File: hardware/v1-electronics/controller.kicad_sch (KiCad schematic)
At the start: 35 parts, among them IC1 IS31FL3733-QFLS4-TR, IC2 IS31FL3733-QFLS4-TR, J2 Conn_01x03, U1 MDBT50Q-1MV2

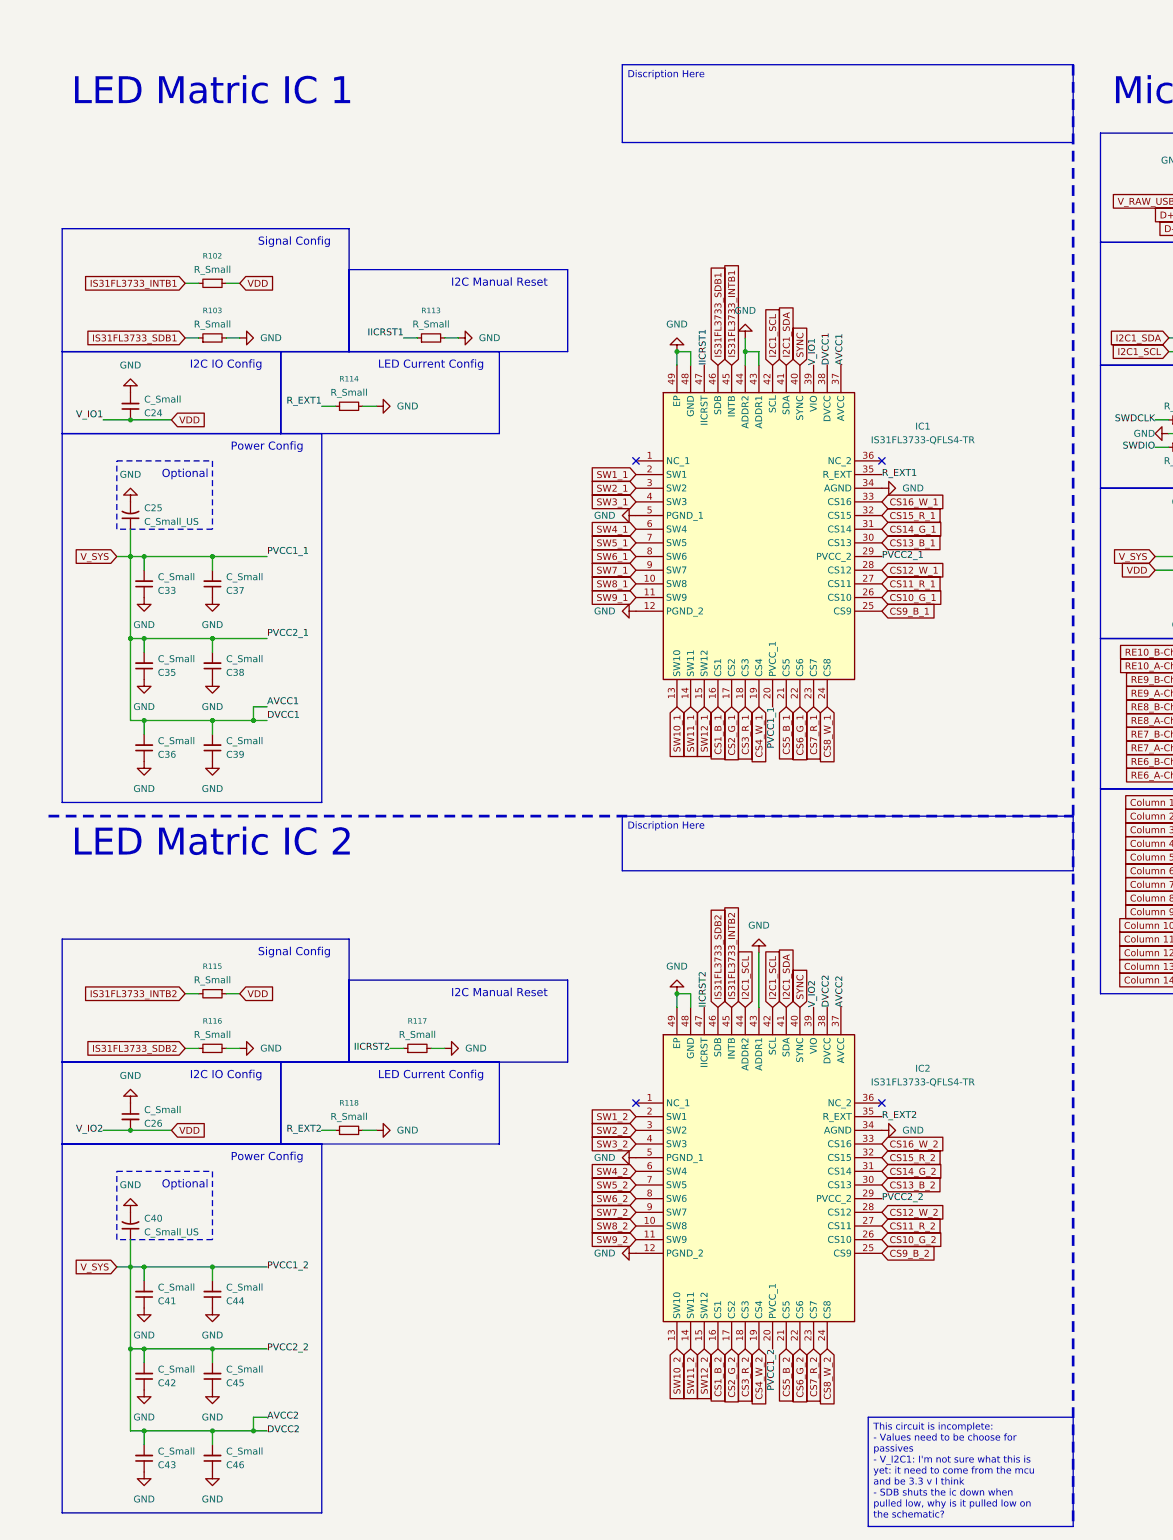
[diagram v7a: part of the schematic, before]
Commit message: fix(v1 hardware): fixed the matrix circuit
the change in LED Matrix Driver results in a need to change how we
wire the matrix. this diff accounts for that.

i needed to use a script to rename labels.
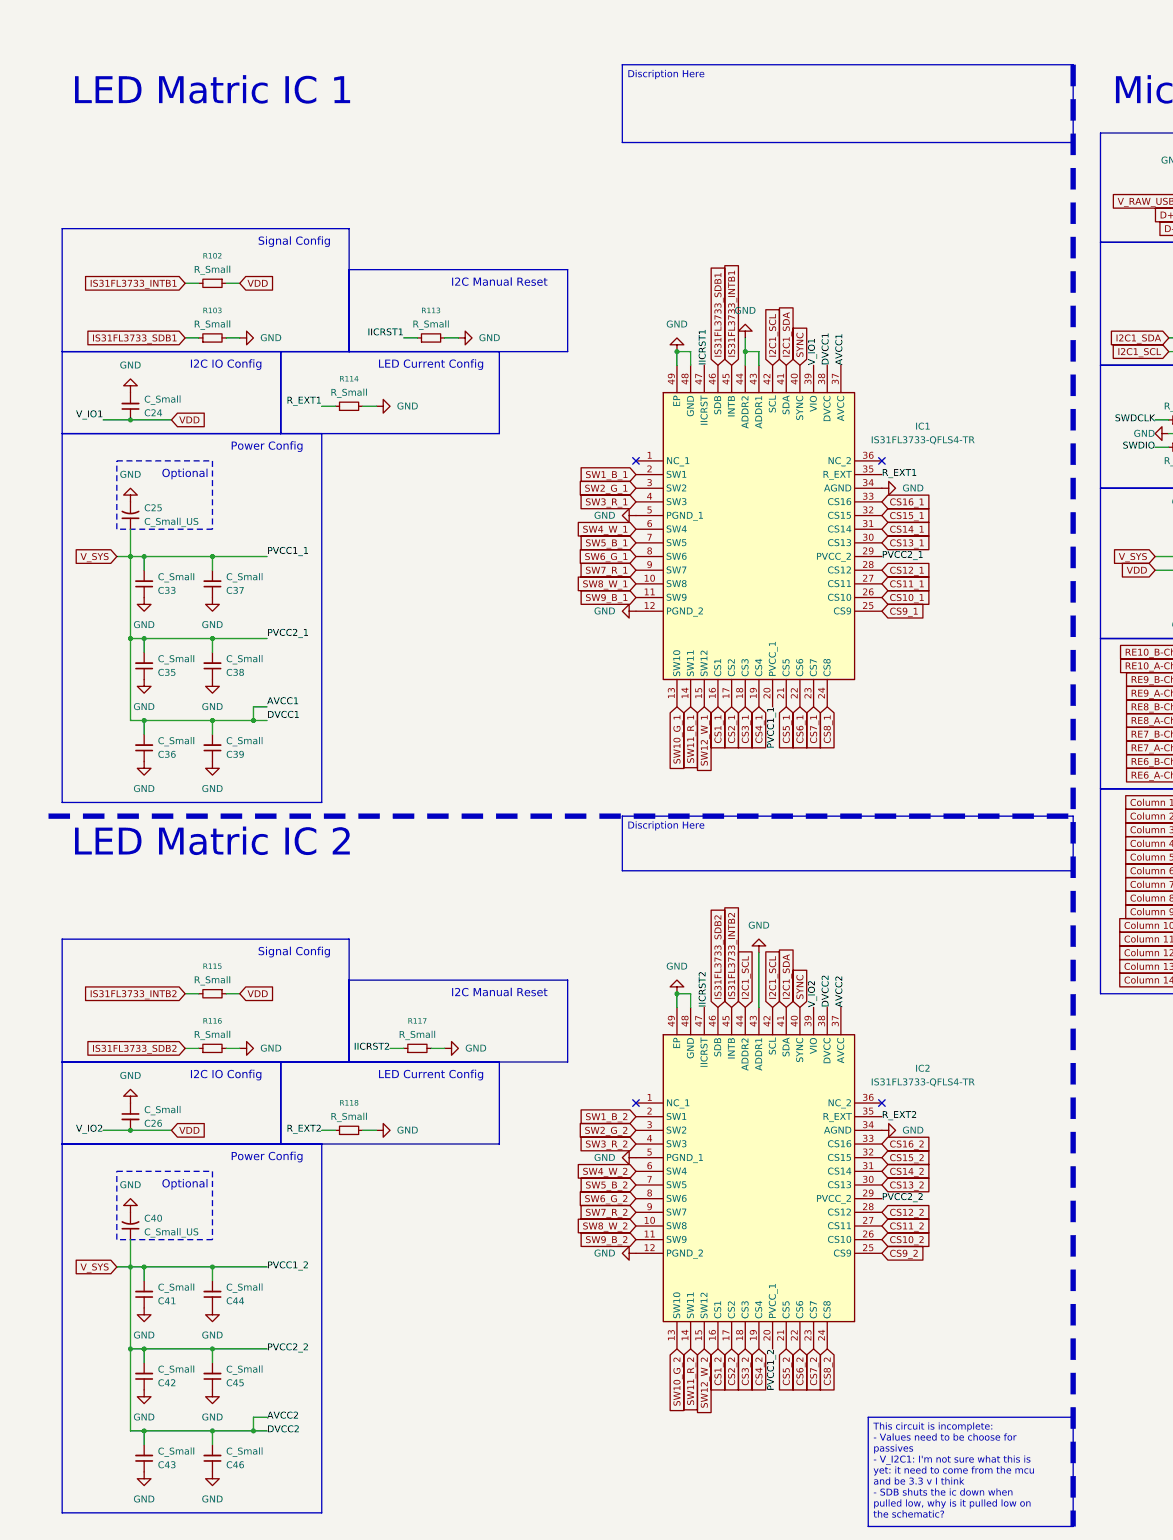
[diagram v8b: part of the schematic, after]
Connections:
- net CS10_G_1 renamed CS10_1
- net CS10_G_2 renamed CS10_2
- net CS11_R_1 renamed CS11_1
- net CS11_R_2 renamed CS11_2
- net CS12_W_1 renamed CS12_1
- net CS12_W_2 renamed CS12_2
- net CS13_B_1 renamed CS13_1
- net CS13_B_2 renamed CS13_2
- net CS14_G_1 renamed CS14_1
- net CS14_G_2 renamed CS14_2
- net CS15_R_1 renamed CS15_1
- net CS15_R_2 renamed CS15_2
- net CS16_W_1 renamed CS16_1
- net CS16_W_2 renamed CS16_2
- net CS1_B_1 renamed CS1_1
- net CS1_B_2 renamed CS1_2
- net CS2_G_1 renamed CS2_1
- net CS2_G_2 renamed CS2_2
- net CS3_R_1 renamed CS3_1
- net CS3_R_2 renamed CS3_2
- net CS4_W_1 renamed CS4_1
- net CS4_W_2 renamed CS4_2
- net CS5_B_1 renamed CS5_1
- net CS5_B_2 renamed CS5_2
- net CS6_G_1 renamed CS6_1
- net CS6_G_2 renamed CS6_2
- net CS7_R_1 renamed CS7_1
- net CS7_R_2 renamed CS7_2
- net CS8_W_1 renamed CS8_1
- net CS8_W_2 renamed CS8_2
- net CS9_B_1 renamed CS9_1
- net CS9_B_2 renamed CS9_2
- net SW10_1 renamed SW10_G_1
- net SW10_2 renamed SW10_G_2
- net SW11_1 renamed SW11_R_1
- net SW11_2 renamed SW11_R_2
- net SW12_1 renamed SW12_W_1
- net SW12_2 renamed SW12_W_2
- net SW1_1 renamed SW1_B_1
- net SW1_2 renamed SW1_B_2
- net SW2_1 renamed SW2_G_1
- net SW2_2 renamed SW2_G_2
- net SW3_1 renamed SW3_R_1
- net SW3_2 renamed SW3_R_2
- net SW4_1 renamed SW4_W_1
- net SW4_2 renamed SW4_W_2
- net SW5_1 renamed SW5_B_1
- net SW5_2 renamed SW5_B_2
- net SW6_1 renamed SW6_G_1
- net SW6_2 renamed SW6_G_2
- net SW7_1 renamed SW7_R_1
- net SW7_2 renamed SW7_R_2
- net SW8_1 renamed SW8_W_1
- net SW8_2 renamed SW8_W_2
- net SW9_1 renamed SW9_B_1
- net SW9_2 renamed SW9_B_2
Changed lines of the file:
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@@
 		)
 		(stroke
-			(width 0.5)
+			(width 1)
 			(type dash_dot_dot)
 		)
@@
 		)
 		(stroke
-			(width 0.5)
+			(width 1)
 			(type dash_dot_dot)
 		)
@@
 		)
 	)
-	(global_label "CS7_R_1"
+	(global_label "CS7_1"
 		(shape input)
 		(at 154.94 132.08 270)
@@
 		)
 	)
-	(global_label "CS12_W_2"
+	(global_label "CS12_2"
 		(shape input)
 		(at 167.64 226.06 0)
@@
 		)
 	)
-	(global_label "SW7_1"
+	(global_label "SW7_R_1"
 		(shape input)
 		(at 121.92 106.68 180)
@@
 		)
 	)
-	(global_label "CS4_W_2"
+	(global_label "CS4_2"
 		(shape input)
 		(at 144.78 251.46 270)
@@
 		)
 	)
-	(global_label "CS11_R_1"
+	(global_label "CS11_1"
 		(shape input)
 		(at 167.64 109.22 0)
@@
 		)
 	)
-	(global_label "SW10_2"
+	(global_label "SW10_G_2"
 		(shape input)
 		(at 129.54 251.46 270)
@@
 		)
 	)
-	(global_label "CS14_G_2"
+	(global_label "CS14_2"
 		(shape input)
 		(at 167.64 218.44 0)
@@
 		)
 	)
-	(global_label "CS8_W_2"
+	(global_label "CS8_2"
 		(shape input)
 		(at 157.48 251.46 270)
@@
 		)
 	)
-	(global_label "CS10_G_2"
+	(global_label "CS10_2"
 		(shape input)
 		(at 167.64 231.14 0)
@@
 		)
 	)
-	(global_label "CS14_G_1"
+	(global_label "CS14_1"
 		(shape input)
 		(at 167.64 99.06 0)
@@
 		)
 	)
-	(global_label "CS16_W_2"
+	(global_label "CS16_2"
 		(shape input)
 		(at 167.64 213.36 0)
@@
 		)
 	)
-	(global_label "CS4_W_1"
+	(global_label "CS4_1"
 		(shape input)
 		(at 144.78 132.08 270)
@@
 		)
 	)
-	(global_label "CS1_B_1"
+	(global_label "CS1_1"
 		(shape input)
 		(at 137.16 132.08 270)
@@
 		)
 	)
-	(global_label "CS7_R_2"
+	(global_label "CS7_2"
 		(shape input)
 		(at 154.94 251.46 270)
@@
 		)
 	)
-	(global_label "SW7_2"
+	(global_label "SW7_R_2"
 		(shape input)
 		(at 121.92 226.06 180)
@@
 		)
 	)
-	(global_label "SW4_1"
+	(global_label "SW4_W_1"
 		(shape input)
 		(at 121.92 99.06 180)
@@
 		)
 	)
-	(global_label "CS13_B_2"
+	(global_label "CS13_2"
 		(shape input)
 		(at 167.64 220.98 0)
@@
 		)
 	)
-	(global_label "SW12_1"
+	(global_label "SW12_W_1"
 		(shape input)
 		(at 134.62 132.08 270)
@@
 		)
 	)
-	(global_label "SW8_1"
+	(global_label "SW8_W_1"
 		(shape input)
 		(at 121.92 109.22 180)
@@
 		)
 	)
-	(global_label "CS3_R_2"
+	(global_label "CS3_2"
 		(shape input)
 		(at 142.24 251.46 270)
@@
 		)
 	)
-	(global_label "SW5_2"
+	(global_label "SW5_B_2"
 		(shape input)
 		(at 121.92 220.98 180)
@@
 		)
 	)
-	(global_label "SW9_2"
+	(global_label "SW9_B_2"
 		(shape input)
 		(at 121.92 231.14 180)
@@
 		)
 	)
-	(global_label "SW11_1"
+	(global_label "SW11_R_1"
 		(shape input)
 		(at 132.08 132.08 270)
@@
 		)
 	)
-	(global_label "SW3_1"
+	(global_label "SW3_R_1"
 		(shape input)
 		(at 121.92 93.98 180)
@@
 		)
 	)
-	(global_label "CS2_G_1"
+	(global_label "CS2_1"
 		(shape input)
 		(at 139.7 132.08 270)
@@
 		)
 	)
-	(global_label "CS11_R_2"
+	(global_label "CS11_2"
 		(shape input)
 		(at 167.64 228.6 0)
@@
 		)
 	)
-	(global_label "CS5_B_1"
+	(global_label "CS5_1"
 		(shape input)
 		(at 149.86 132.08 270)
@@
 		)
 	)
-	(global_label "SW6_2"
+	(global_label "SW6_G_2"
 		(shape input)
 		(at 121.92 223.52 180)
@@
 		)
 	)
-	(global_label "CS1_B_2"
+	(global_label "CS1_2"
 		(shape input)
 		(at 137.16 251.46 270)
@@
 		)
 	)
-	(global_label "SW1_1"
+	(global_label "SW1_B_1"
 		(shape input)
 		(at 121.92 88.9 180)
@@
 		)
 	)
-	(global_label "CS3_R_1"
+	(global_label "CS3_1"
 		(shape input)
 		(at 142.24 132.08 270)
@@
 		)
 	)
-	(global_label "CS10_G_1"
+	(global_label "CS10_1"
 		(shape input)
 		(at 167.64 111.76 0)
@@
 		)
 	)
-	(global_label "SW1_2"
+	(global_label "SW1_B_2"
 		(shape input)
 		(at 121.92 208.28 180)
@@
 		)
 	)
-	(global_label "SW2_2"
+	(global_label "SW2_G_2"
 		(shape input)
 		(at 121.92 210.82 180)
@@
 		)
 	)
-	(global_label "CS6_G_2"
+	(global_label "CS6_2"
 		(shape input)
 		(at 152.4 251.46 270)
@@
 		)
 	)
-	(global_label "CS2_G_2"
+	(global_label "CS2_2"
 		(shape input)
 		(at 139.7 251.46 270)
@@
 		)
 	)
-	(global_label "CS15_R_1"
+	(global_label "CS15_1"
 		(shape input)
 		(at 167.64 96.52 0)
@@
 		)
 	)
-	(global_label "CS12_W_1"
+	(global_label "CS12_1"
 		(shape input)
 		(at 167.64 106.68 0)
@@
 		)
 	)
-	(global_label "CS5_B_2"
+	(global_label "CS5_2"
 		(shape input)
 		(at 149.86 251.46 270)
@@
 		)
 	)
-	(global_label "SW10_1"
+	(global_label "SW10_G_1"
 		(shape input)
 		(at 129.54 132.08 270)
@@
 		)
 	)
-	(global_label "SW8_2"
+	(global_label "SW8_W_2"
 		(shape input)
 		(at 121.92 228.6 180)
@@
 		)
 	)
-	(global_label "CS9_B_2"
+	(global_label "CS9_2"
 		(shape input)
 		(at 167.64 233.68 0)
@@
 		)
 	)
-	(global_label "SW6_1"
+	(global_label "SW6_G_1"
 		(shape input)
 		(at 121.92 104.14 180)
@@
 		)
 	)
-	(global_label "SW9_1"
+	(global_label "SW9_B_1"
 		(shape input)
 		(at 121.92 111.76 180)
@@
 		)
 	)
-	(global_label "CS6_G_1"
+	(global_label "CS6_1"
 		(shape input)
 		(at 152.4 132.08 270)
@@
 		)
 	)
-	(global_label "SW12_2"
+	(global_label "SW12_W_2"
 		(shape input)
 		(at 134.62 251.46 270)
@@
 		)
 	)
-	(global_label "CS13_B_1"
+	(global_label "CS13_1"
 		(shape input)
 		(at 167.64 101.6 0)
@@
 		)
 	)
-	(global_label "CS8_W_1"
+	(global_label "CS8_1"
 		(shape input)
 		(at 157.48 132.08 270)
@@
 		)
 	)
-	(global_label "SW11_2"
+	(global_label "SW11_R_2"
 		(shape input)
 		(at 132.08 251.46 270)
@@
 		)
 	)
-	(global_label "SW3_2"
+	(global_label "SW3_R_2"
 		(shape input)
 		(at 121.92 213.36 180)
@@
 		)
 	)
-	(global_label "SW2_1"
+	(global_label "SW2_G_1"
 		(shape input)
 		(at 121.92 91.44 180)
@@
 		)
 	)
-	(global_label "CS15_R_2"
+	(global_label "CS15_2"
 		(shape input)
 		(at 167.64 215.9 0)
@@
 		)
 	)
-	(global_label "SW5_1"
+	(global_label "SW5_B_1"
 		(shape input)
 		(at 121.92 101.6 180)
@@
 		)
 	)
-	(global_label "CS9_B_1"
+	(global_label "CS9_1"
 		(shape input)
 		(at 167.64 114.3 0)
@@
 		)
 	)
-	(global_label "SW4_2"
+	(global_label "SW4_W_2"
 		(shape input)
 		(at 121.92 218.44 180)
@@
 		)
 	)
-	(global_label "CS16_W_1"
+	(global_label "CS16_1"
 		(shape input)
 		(at 167.64 93.98 0)
